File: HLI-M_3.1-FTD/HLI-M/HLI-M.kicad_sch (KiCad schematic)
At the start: 119 parts, among them CON1 , CON2 USB_B, CON3 , CON4 Con_ADAPTER, CON5 Con_MULTLINKER, CON6 Conn_01x15, CON7 Conn_01x09, CON8 CR123A, Q1 DMP3068L-7, Q2 BC817, Q3 BC817, Q4 DMP2305, Q5 DMP2305, Q6 DMP2305, Q7 DMP2305, U1 PIC24HJ64GP206, U10 ULN2003, U11 ULN2003, U12 ULN2003, U2 FM25V10, U3 MAX3232, U4 ATSHA204A-SSHDA-B, U5 24AA02-OT, U6 LM3658SD, U7 TPS7A0533PDBV, U8 TPS7A0533PDBV, U9 FT232RL, Y1 Crystal_32KHz, Y2 Crystal_20MHz

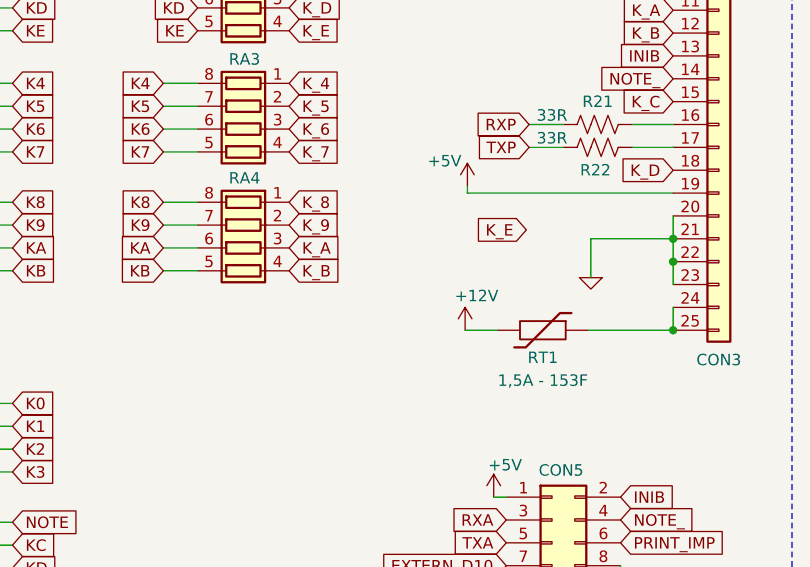
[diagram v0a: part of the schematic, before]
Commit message: atualização serigrafia e conector bateria
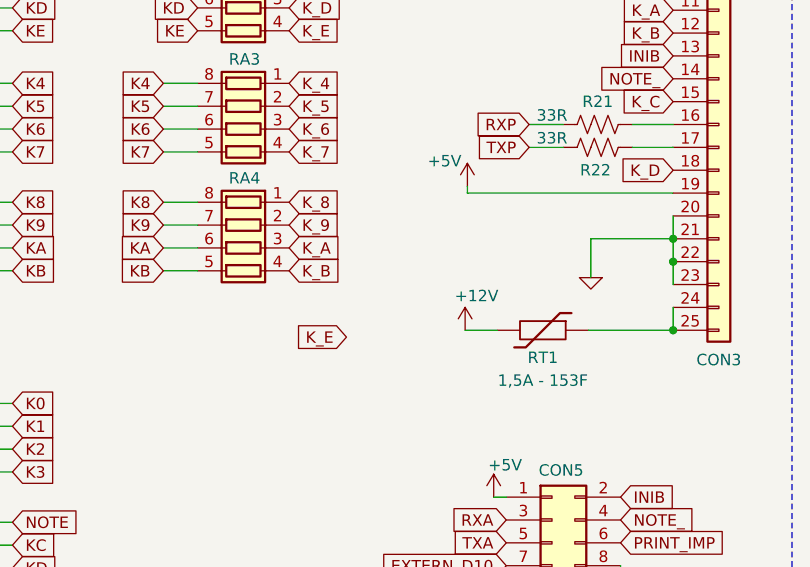
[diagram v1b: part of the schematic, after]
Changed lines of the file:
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@@
     )
   )
-  (global_label "K_E" (shape input) (at 454.3552 84.8614 180) (fields_autoplaced)
+  (global_label "K_E" (shape input) (at 434.3654 96.774 180) (fields_autoplaced)
     (effects (font (size 1.27 1.27)) (justify right))
-    (property "Intersheetrefs" "${INTERSHEET_REFS}" (at 448.6443 84.782 0)
+    (property "Intersheetrefs" "${INTERSHEET_REFS}" (at 428.6545 96.6946 0)
       (effects (font (size 1.27 1.27)) (justify right) hide)
     )

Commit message: Update HLI-M.kicad_sch
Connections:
- net 0: no longer CON3.20 (Pin_20)
- net K_E: now also CON3.20 (Pin_20)
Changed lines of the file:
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@@
-    (stroke (width 0) (type default))
-  )
-  (wire (pts (xy 470.662 83.312) (xy 470.662 85.852))
     (stroke (width 0) (type default))
   )
@@
     )
   )
-  (global_label "K_E" (shape input) (at 434.3654 96.774 180) (fields_autoplaced)
+  (global_label "K_E" (shape input) (at 470.662 83.312 180) (fields_autoplaced)
     (effects (font (size 1.27 1.27)) (justify right))
-    (property "Intersheetrefs" "${INTERSHEET_REFS}" (at 428.6545 96.6946 0)
+    (property "Intersheetrefs" "${INTERSHEET_REFS}" (at 464.9511 83.2326 0)
       (effects (font (size 1.27 1.27)) (justify right) hide)
     )

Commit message: att
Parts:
- removed CON5: Con_MULTLINKER, Connector_IDC:IDC-Header_2x04_P2.54mm_Horizontal, symbol Connector_Generic:Conn_02x04_Odd_Even
- added CON5: Con_MULTLINKER, Connector_IDC:IDC-Header_2x05_P2.54mm_Horizontal, symbol Connector_Generic:Conn_02x05_Odd_Even
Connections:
- net +5V: now also CON5.1 (Pin_1)
- net 0: now also CON5.10 (Pin_10), CON5.9 (Pin_9)
- net EXTERN_D10: now also CON5.7 (Pin_7)
- net INIB: now also CON5.2 (Pin_2)
- net NOTE_: now also CON5.4 (Pin_4)
- net PRINT_IMP: now also CON5.6 (Pin_6)
- net RXA: now also CON5.3 (Pin_3)
- net TXA: now also CON5.5 (Pin_5)
- net EXTERN_D11: now reaches U1.45 (RD11)
- net EXTERN_D11: now also CON5.8 (Pin_8)
- no-connect marks 35 -> 34
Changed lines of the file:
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@@
   (no_connect (at 77.47 286.258))
   (no_connect (at 132.842 215.392))
-  (no_connect (at 201.168 90.17))
   (no_connect (at 286.258 72.39))
   (no_connect (at 118.11 291.338))
@@
     (stroke (width 0) (type default))
   )
-  (wire (pts (xy 464.82 125.984) (xy 464.82 122.174))
-    (stroke (width 0) (type default))
-  )
   (wire (pts (xy 378.714 117.348) (xy 383.286 117.348))
     (stroke (width 0) (type default))
@@
     (stroke (width 0) (type default))
   )
+  (wire (pts (xy 452.12 125.984) (xy 452.12 124.46))
+    (stroke (width 0) (type default))
+  )
   (wire (pts (xy 392.684 214.122) (xy 392.684 218.186))
     (stroke (width 0) (type default))
@@
     (stroke (width 0) (type default))
   )
+  (wire (pts (xy 464.82 125.984) (xy 464.82 124.46))
+    (stroke (width 0) (type default))
+  )
   (wire (pts (xy 472.44 212.09) (xy 455.422 212.09))
     (stroke (width 0) (type default))
@@
     (stroke (width 0) (type default))
   )
-  (wire (pts (xy 450.723 114.554) (xy 452.12 114.554))
+  (wire (pts (xy 450.215 114.3) (xy 452.12 114.3))
     (stroke (width 0) (type default))
   )
@@
     (stroke (width 0) (type default))
   )
+  (wire (pts (xy 450.215 114.3) (xy 450.215 113.919))
+    (stroke (width 0) (type default))
+  )
   (wire (pts (xy 417.83 68.58) (xy 414.02 68.58))
     (stroke (width 0) (type default))
@@
     )
   )
+  (global_label "EXTERN_D11" (shape input) (at 464.82 121.92 0) (fields_autoplaced)
+    (effects (font (size 1.27 1.27)) (justify left))
+    (property "Intersheetrefs" "${INTERSHEET_REFS}" (at 478.8038 121.92 0)
+      (effects (font (size 1.27 1.27)) (justify left) hide)
+    )
+  )
   (global_label "K6" (shape input) (at 397.256 73.66 0) (fields_autoplaced)
     (effects (font (size 1.27 1.27)) (justify left))
@@
     )
   )
-  (global_label "TXA" (shape input) (at 452.12 119.634 180) (fields_autoplaced)
+  (global_label "TXA" (shape input) (at 452.12 119.38 180) (fields_autoplaced)
     (effects (font (size 1.27 1.27)) (justify right))
-    (property "Intersheetrefs" "${INTERSHEET_REFS}" (at 590.55 476.504 0)
+    (property "Intersheetrefs" "${INTERSHEET_REFS}" (at 590.55 476.25 0)
       (effects (font (size 1.27 1.27)) hide)
     )
@@
     )
   )
-  (global_label "RXA" (shape input) (at 452.12 117.094 180) (fields_autoplaced)
+  (global_label "RXA" (shape input) (at 452.12 116.84 180) (fields_autoplaced)
     (effects (font (size 1.27 1.27)) (justify right))
-    (property "Intersheetrefs" "${INTERSHEET_REFS}" (at 590.55 463.804 0)
+    (property "Intersheetrefs" "${INTERSHEET_REFS}" (at 590.55 463.55 0)
       (effects (font (size 1.27 1.27)) hide)
     )
@@
     )
   )
+  (global_label "EXTERN_D11" (shape input) (at 201.168 90.17 180) (fields_autoplaced)
+    (effects (font (size 1.27 1.27)) (justify right))
+    (property "Intersheetrefs" "${INTERSHEET_REFS}" (at 187.1842 90.17 0)
+      (effects (font (size 1.27 1.27)) (justify right) hide)
+    )
+  )
   (global_label "K6" (shape input) (at 397.51 135.636 0) (fields_autoplaced)
     (effects (font (size 1.27 1.27)) (justify left))
@@
     )
   )
-  (global_label "PRINT_IMP" (shape input) (at 464.82 119.634 0) (fields_autoplaced)
+  (global_label "PRINT_IMP" (shape input) (at 464.82 119.38 0) (fields_autoplaced)
     (effects (font (size 1.27 1.27)) (justify left))
-    (property "Intersheetrefs" "${INTERSHEET_REFS}" (at 996.95 270.764 0)
+    (property "Intersheetrefs" "${INTERSHEET_REFS}" (at 996.95 270.51 0)
       (effects (font (size 1.27 1.27)) hide)
     )
@@
     )
   )
-  (global_label "NOTE_" (shape input) (at 464.82 117.094 0) (fields_autoplaced)
+  (global_label "NOTE_" (shape input) (at 464.82 116.84 0) (fields_autoplaced)
     (effects (font (size 1.27 1.27)) (justify left))
-    (property "Intersheetrefs" "${INTERSHEET_REFS}" (at 1026.16 157.734 0)
+    (property "Intersheetrefs" "${INTERSHEET_REFS}" (at 1026.16 157.48 0)
       (effects (font (size 1.27 1.27)) hide)
     )
@@
     )
   )
-  (global_label "INIB" (shape input) (at 464.82 114.554 0) (fields_autoplaced)
+  (global_label "INIB" (shape input) (at 464.82 114.3 0) (fields_autoplaced)
     (effects (font (size 1.27 1.27)) (justify left))
-    (property "Intersheetrefs" "${INTERSHEET_REFS}" (at 1026.16 180.594 0)
+    (property "Intersheetrefs" "${INTERSHEET_REFS}" (at 1026.16 180.34 0)
       (effects (font (size 1.27 1.27)) hide)
     )
@@
     )
   )
-  (global_label "EXTERN_D10" (shape input) (at 452.12 122.174 180) (fields_autoplaced)
+  (global_label "EXTERN_D10" (shape input) (at 452.12 121.92 180) (fields_autoplaced)
     (effects (font (size 1.27 1.27)) (justify right))
-    (property "Intersheetrefs" "${INTERSHEET_REFS}" (at 438.0634 122.0946 0)
+    (property "Intersheetrefs" "${INTERSHEET_REFS}" (at 438.0634 121.8406 0)
       (effects (font (size 1.27 1.27)) (justify right) hide)
     )
@@
     )
   )
+  (symbol (lib_id "Connector_Generic:Conn_02x05_Odd_Even") (at 457.2 119.38 0) (unit 1)
+    (in_bom yes) (on_board yes) (dnp no)
+    (property "Reference" "CON5" (at 458.343 111.379 0)
+      (effects (font (size 1.27 1.27)))
+    )
+    (property "Value" "Con_MULTLINKER" (at 458.089 129.921 0)
+      (effects (font (size 1.27 1.27)))
+    )
+    (property "Footprint" "Connector_IDC:IDC-Header_2x05_P2.54mm_Horizontal" (at 457.2 119.38 0)
+      (effects (font (size 1.27 1.27)) hide)
+    )
+    (property "Datasheet" "~" (at 457.2 119.38 0)
+      (effects (font (size 1.27 1.27)) hide)
+    )
+    (pin "1")
+    (pin "10")
+    (pin "2")
+    (pin "3")
+    (pin "4")
+    (pin "5")
+    (pin "6")
+    (pin "7")
+    (pin "8")
+    (pin "9")
+    (instances
+      (project "HLI-M"
+        (path "/869d6302-ae22-478f-9723-3feacbb12eef"
+          (reference "CON5") (unit 1)
+        )
+      )
+    )
+  )
   (symbol (lib_id "Device:D") (at 69.2912 234.95 180) (unit 1)
     (in_bom yes) (on_board yes) (dnp no) (fields_autoplaced)
@@
     )
   )
-  (symbol (lib_id "power:+5V") (at 450.723 114.554 0) (unit 1)
+  (symbol (lib_id "power:+5V") (at 450.215 113.919 0) (unit 1)
     (in_bom yes) (on_board yes) (dnp no)
-    (property "Reference" "#PWR0102" (at 450.723 118.364 0)
+    (property "Reference" "#PWR0102" (at 450.215 117.729 0)
       (effects (font (size 1.27 1.27)) hide)
     )
-    (property "Value" "+5V" (at 451.993 110.998 0)
+    (property "Value" "+5V" (at 451.485 110.363 0)
       (effects (font (size 1.27 1.27)))
     )
-    (property "Footprint" "" (at 450.723 114.554 0)
+    (property "Footprint" "" (at 450.215 113.919 0)
       (effects (font (size 1.27 1.27)) hide)
     )
-    (property "Datasheet" "" (at 450.723 114.554 0)
+    (property "Datasheet" "" (at 450.215 113.919 0)
       (effects (font (size 1.27 1.27)) hide)
     )
@@
     )
   )
+  (symbol (lib_id "pspice:0") (at 452.12 125.984 0) (unit 1)
+    (in_bom yes) (on_board yes) (dnp no)
+    (property "Reference" "#GND03" (at 452.12 128.524 0)
+      (effects (font (size 1.27 1.27)) hide)
+    )
+    (property "Value" "0" (at 452.12 123.7234 0)
+      (effects (font (size 1.27 1.27)) hide)
+    )
+    (property "Footprint" "" (at 452.12 125.984 0)
+      (effects (font (size 1.27 1.27)) hide)
+    )
+    (property "Datasheet" "~" (at 452.12 125.984 0)
+      (effects (font (size 1.27 1.27)) hide)
+    )
+    (pin "1")
+    (instances
+      (project "HLI-M"
+        (path "/869d6302-ae22-478f-9723-3feacbb12eef"
+          (reference "#GND03") (unit 1)
+        )
+      )
+    )
+  )
   (symbol (lib_id "pspice:0") (at 464.82 125.984 0) (unit 1)
     (in_bom yes) (on_board yes) (dnp no)
@@
         )
       )
-    )
-  )
-  (symbol (lib_id "Connector_Generic:Conn_02x04_Odd_Even") (at 457.2 117.094 0) (unit 1)
-    (in_bom yes) (on_board yes) (dnp no)
-    (property "Reference" "CON5" (at 458.216 111.5822 0)
-      (effects (font (size 1.27 1.27)))
-    )
-    (property "Value" "Con_MULTLINKER" (at 452.882 126.238 0)
-      (effects (font (size 1.27 1.27)))
-    )
-    (property "Footprint" "Connector_IDC:IDC-Header_2x04_P2.54mm_Horizontal" (at 457.2 117.094 0)
-      (effects (font (size 1.27 1.27)) hide)
-    )
-    (property "Datasheet" "~" (at 457.2 117.094 0)
-      (effects (font (size 1.27 1.27)) hide)
-    )
-    (pin "1")
-    (pin "2")
-    (pin "3")
-    (pin "4")
-    (pin "5")
-    (pin "6")
-    (pin "7")
-    (pin "8")
-    (instances
-      (project "HLI-M"
-        (path "/869d6302-ae22-478f-9723-3feacbb12eef"
-          (reference "CON5") (unit 1)
-        )
-      )

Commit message: att
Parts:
- added Q8: BC817, Package_TO_SOT_SMD:SOT-23, symbol Transistor_BJT:BC817
- added R31: 22K, Resistor_SMD:R_0603_1608Metric_Pad0.98x0.95mm_HandSolder, symbol Device:R
- added R32: 1K, Resistor_SMD:R_0603_1608Metric_Pad0.98x0.95mm_HandSolder, symbol Device:R
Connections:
- net +3V3: now also R32.1
- net 0: now also CON3.20 (Pin_20), Q8.2 (E); no longer CON3.22 (Pin_22)
- net EXTERN_D11: now also Q8.3 (C), R32.2; no longer CON5.8 (Pin_8)
- net K_E: now also CON3.22 (Pin_22); no longer CON3.20 (Pin_20)
- new net: Q8.1 (B), R31.1
- new net D11_IC: CON5.8 (Pin_8), R31.2
- no-connect marks 34 -> 33

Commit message: att
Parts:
- added R33: NC, Resistor_SMD:R_0603_1608Metric_Pad0.98x0.95mm_HandSolder, symbol Device:R
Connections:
- net +12V: now also CON5.10 (Pin_10)
- net +5VD: now also R33.1
- net 0: no longer CON5.10 (Pin_10)
- net D11_IC renamed HOOPER_
- net HOOPER_: now also R33.2
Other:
- note added: "IMPRESSORA, NOTEIRO, HOOPER e MOEDEIRO."
- note removed: "IMPRESSORA E NOTEIRO."
- moved on the sheet: CON5, Q2, Q8, R17, R18, R31, R32, U5

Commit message: att
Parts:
- removed RV1: Varistor, Capacitor_SMD:C_0603_1608Metric_Pad1.08x0.95mm_HandSolder, symbol Device:Varistor
- added D6: MMSZ5233B, symbol Device:D_Zener
- F1: value Fuse -> 0.12A 30V
- R33: value NC -> 0R
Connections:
- net +5V: now also D6.1 (K)
- net 0: now also D6.2 (A)
- no-connect marks 33 -> 46
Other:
- moved on the sheet: F1
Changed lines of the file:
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@@
   (junction (at 234.188 153.67) (diameter 0) (color 0 0 0 0)
   )
+  (junction (at 60.706 196.342) (diameter 0) (color 0 0 0 0)
+  )
   (junction (at 378.714 86.868) (diameter 0) (color 0 0 0 0)
   )
@@
   (junction (at 136.906 34.29) (diameter 0) (color 0 0 0 0)
   )
-  (junction (at 60.7314 187.8584) (diameter 0) (color 0 0 0 0)
-  )
   (junction (at 378.714 46.736) (diameter 0) (color 0 0 0 0)
   )
@@
   (junction (at 298.45 104.14) (diameter 0) (color 0 0 0 0)
   )
+  (junction (at 60.706 187.96) (diameter 0) (color 0 0 0 0)
+  )
   (junction (at 38.862 290.576) (diameter 0) (color 0 0 0 0)
   )
@@
   (junction (at 212.09 196.342) (diameter 0) (color 0 0 0 0)
   )
-  (junction (at 60.706 196.3674) (diameter 0) (color 0 0 0 0)
-  )
   (junction (at 168.402 181.864) (diameter 0) (color 0 0 0 0)
   )
@@
   (junction (at 161.036 181.864) (diameter 0) (color 0 0 0 0)
   )
+  (no_connect (at 322.58 119.38))
   (no_connect (at 371.094 223.266))
+  (no_connect (at 83.566 150.114))
+  (no_connect (at 64.643 124.333))
+  (no_connect (at 329.184 87.503))
   (no_connect (at 430.784 224.79))
   (no_connect (at 118.11 273.558))
@@
   (no_connect (at 77.47 286.258))
   (no_connect (at 132.842 215.392))
+  (no_connect (at 470.662 113.538))
   (no_connect (at 286.258 72.39))
   (no_connect (at 118.11 291.338))
   (no_connect (at 326.898 82.55))
+  (no_connect (at 105.283 171.831))
+  (no_connect (at 52.959 66.675))
   (no_connect (at 350.774 225.806))
+  (no_connect (at 475.742 121.412))
   (no_connect (at 430.784 227.33))
+  (no_connect (at 291.973 171.45))
   (no_connect (at 326.898 72.39))
   (no_connect (at 132.842 219.202))
@@
   (no_connect (at 371.094 225.806))
   (no_connect (at 350.774 228.346))
+  (no_connect (at 298.196 236.601))
   (no_connect (at 472.44 217.17))
+  (no_connect (at 277.241 286.258))
   (no_connect (at 77.47 281.178))
+  (no_connect (at 50.292 27.178))
   (no_connect (at 118.11 293.878))
   (no_connect (at 118.11 298.958))
@@
   (no_connect (at 451.358 152.4))
   (no_connect (at 451.358 154.94))
+  (no_connect (at 63.627 90.551))
   (no_connect (at 118.11 288.798))
   (no_connect (at 371.094 228.346))
@@
     (stroke (width 0) (type default))
   )
-  (wire (pts (xy 60.7314 196.3674) (xy 60.706 196.3674))
-    (stroke (width 0) (type default))
-  )
   (wire (pts (xy 303.784 124.968) (xy 317.5 124.968))
     (stroke (width 0) (type default))
@@
     (stroke (width 0) (type default))
   )
-  (wire (pts (xy 275.59 193.294) (xy 275.59 192.024))
+  (wire (pts (xy 69.85 187.96) (xy 69.85 190.1952))
     (stroke (width 0) (type default))
   )
-  (wire (pts (xy 60.706 196.3674) (xy 60.706 234.95))
+  (wire (pts (xy 275.59 193.294) (xy 275.59 192.024))
     (stroke (width 0) (type default))
   )
@@
     (stroke (width 0) (type default))
   )
+  (wire (pts (xy 60.706 187.96) (xy 69.85 187.96))
+    (stroke (width 0) (type default))
+  )
   (wire (pts (xy 298.704 129.54) (xy 317.5 129.54))
     (stroke (width 0) (type default))
@@
     (stroke (width 0) (type dash))
   )
-  (wire (pts (xy 49.5554 196.3674) (xy 60.706 196.3674))
-    (stroke (width 0) (type default))
-  )
-  (wire (pts (xy 69.85 187.8584) (xy 69.85 190.1952))
+  (wire (pts (xy 53.975 196.342) (xy 60.706 196.342))
     (stroke (width 0) (type default))
   )
@@
     (stroke (width 0) (type dash))
   )
-  (wire (pts (xy 37.2364 196.3674) (xy 41.9354 196.3674))
+  (wire (pts (xy 46.228 196.342) (xy 46.355 196.342))
     (stroke (width 0) (type default))
   )
@@
     (stroke (width 0) (type default))
   )
+  (wire (pts (xy 46.228 196.3674) (xy 37.2364 196.3674))
+    (stroke (width 0) (type default))
+  )
   (wire (pts (xy 138.3284 210.312) (xy 132.842 210.312))
     (stroke (width 0) (type default))
@@
     (stroke (width 0) (type default))
   )
-  (wire (pts (xy 60.7314 195.4784) (xy 60.7314 196.3674))
+  (wire (pts (xy 60.706 195.707) (xy 60.706 196.342))
     (stroke (width 0) (type default))
   )
@@
     (stroke (width 0) (type default))
   )
-  (wire (pts (xy 51.562 187.8584) (xy 51.562 191.2874))
+  (wire (pts (xy 42.926 187.96) (xy 42.926 191.2874))
     (stroke (width 0) (type default))
   )
@@
     (stroke (width 0) (type default))
   )
-  (wire (pts (xy 60.706 196.342) (xy 60.706 196.3674))
+  (wire (pts (xy 60.706 196.342) (xy 60.706 234.95))
     (stroke (width 0) (type default))
   )
@@
     (stroke (width 0) (type default))
   )
-  (wire (pts (xy 430.784 222.25) (xy 430.022 222.25))
+  (wire (pts (xy 60.706 188.087) (xy 60.706 187.96))
     (stroke (width 0) (type default))
   )
-  (wire (pts (xy 65.786 34.798) (xy 65.786 30.226))
+  (wire (pts (xy 430.784 222.25) (xy 430.022 222.25))
     (stroke (width 0) (type default))
   )
-  (wire (pts (xy 51.562 187.8584) (xy 60.7314 187.8584))
+  (wire (pts (xy 65.786 34.798) (xy 65.786 30.226))
     (stroke (width 0) (type default))
   )
@@
     (stroke (width 0) (type default))
   )
-  (wire (pts (xy 38.1762 191.2874) (xy 51.562 191.2874))
+  (wire (pts (xy 38.1762 191.2874) (xy 42.926 191.2874))
     (stroke (width 0) (type default))
   )
@@
     (stroke (width 0) (type default))
   )
+  (wire (pts (xy 46.228 196.342) (xy 46.228 196.3674))
+    (stroke (width 0) (type default))
+  )
   (wire (pts (xy 77.47 263.398) (xy 72.136 263.398))
     (stroke (width 0) (type default))
@@
     (stroke (width 0) (type default))
   )
-  (wire (pts (xy 60.7314 187.8584) (xy 69.85 187.8584))
+  (wire (pts (xy 42.926 187.96) (xy 60.706 187.96))
     (stroke (width 0) (type default))
   )
@@
       (effects (font (size 1.27 1.27)))
     )
-    (property "Value" "NC" (at 43.307 82.677 0)
+    (property "Value" "0R" (at 43.307 82.677 0)
       (effects (font (size 1.27 1.27)))
     )
@@
     )
   )
-  (symbol (lib_id "Device:Varistor") (at 60.7314 191.6684 0) (unit 1)
-    (in_bom yes) (on_board yes) (dnp no)
-    (property "Reference" "RV1" (at 63.119 190.2206 0)
-      (effects (font (size 1.27 1.27)) (justify left))
-    )
-    (property "Value" "Varistor" (at 63.246 192.659 0)
-      (effects (font (size 1.27 1.27)) (justify left))
-    )
-    (property "Footprint" "Capacitor_SMD:C_0603_1608Metric_Pad1.08x0.95mm_HandSolder" (at 58.9534 191.6684 90)
-      (effects (font (size 1.27 1.27)) hide)
-    )
-    (property "Datasheet" "~" (at 60.7314 191.6684 0)
-      (effects (font (size 1.27 1.27)) hide)
-    )
-    (pin "1")
-    (pin "2")
-    (instances
-      (project "HLI-M"
-        (path "/869d6302-ae22-478f-9723-3feacbb12eef"
-          (reference "RV1") (unit 1)
-        )
-      )
-    )
-  )
   (symbol (lib_id "Connector:TestPoint") (at 278.384 252.222 180) (unit 1)
     (in_bom yes) (on_board yes) (dnp no)
@@
     )
   )
-  (symbol (lib_id "Device:Fuse") (at 45.7454 196.3674 90) (unit 1)
+  (symbol (lib_id "Device:Fuse") (at 50.165 196.342 90) (unit 1)
     (in_bom yes) (on_board yes) (dnp no)
-    (property "Reference" "F1" (at 45.6946 194.3862 90)
+    (property "Reference" "F1" (at 50.1142 194.3608 90)
       (effects (font (size 1.27 1.27)))
     )
-    (property "Value" "Fuse" (at 45.7708 198.4756 90)
+    (property "Value" "0.12A 30V" (at 50.1904 198.4502 90)
       (effects (font (size 1.27 1.27)))
     )
-    (property "Footprint" "Fuse:Fuse_1812_4532Metric" (at 45.7454 198.1454 90)
+    (property "Footprint" "Fuse:Fuse_1812_4532Metric" (at 50.165 198.12 90)
       (effects (font (size 1.27 1.27)) hide)
     )
-    (property "Datasheet" "~" (at 45.7454 196.3674 0)
+    (property "Datasheet" "~" (at 50.165 196.342 0)
       (effects (font (size 1.27 1.27)) hide)
     )
@@
         )
       )
+    )
+  )
+  (symbol (lib_id "Device:D_Zener") (at 60.706 191.897 90) (unit 1)
+    (in_bom yes) (on_board yes) (dnp no)
+    (property "Reference" "D6" (at 63.5 190.627 90)
+      (effects (font (size 1.27 1.27)) (justify right))
+    )
+    (property "Value" "MMSZ5233B" (at 62.992 193.04 90)
+      (effects (font (size 1.27 1.27)) (justify right))
+    )
+    (property "Footprint" "" (at 60.706 191.897 0)
+      (effects (font (size 1.27 1.27)) hide)
+    )
+    (property "Datasheet" "~" (at 60.706 191.897 0)
+      (effects (font (size 1.27 1.27)) hide)
+    )
+    (pin "1")
+    (pin "2")
+    (instances
+      (project "HLI-M"
+        (path "/869d6302-ae22-478f-9723-3feacbb12eef"
+          (reference "D6") (unit 1)
+        )
+      )
